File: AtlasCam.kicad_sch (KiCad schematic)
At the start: 36 parts, among them J1 SD_Micro_TFPUSH, J2 USB_C_16Pin_C167321, U1 ESP32-S3-WROOM-1(N8R8), U2 LDO_3V3_2A_AIC1221-33GY3TR, U3 GR6206P282MR-G, U4 GR6206P182MR-G

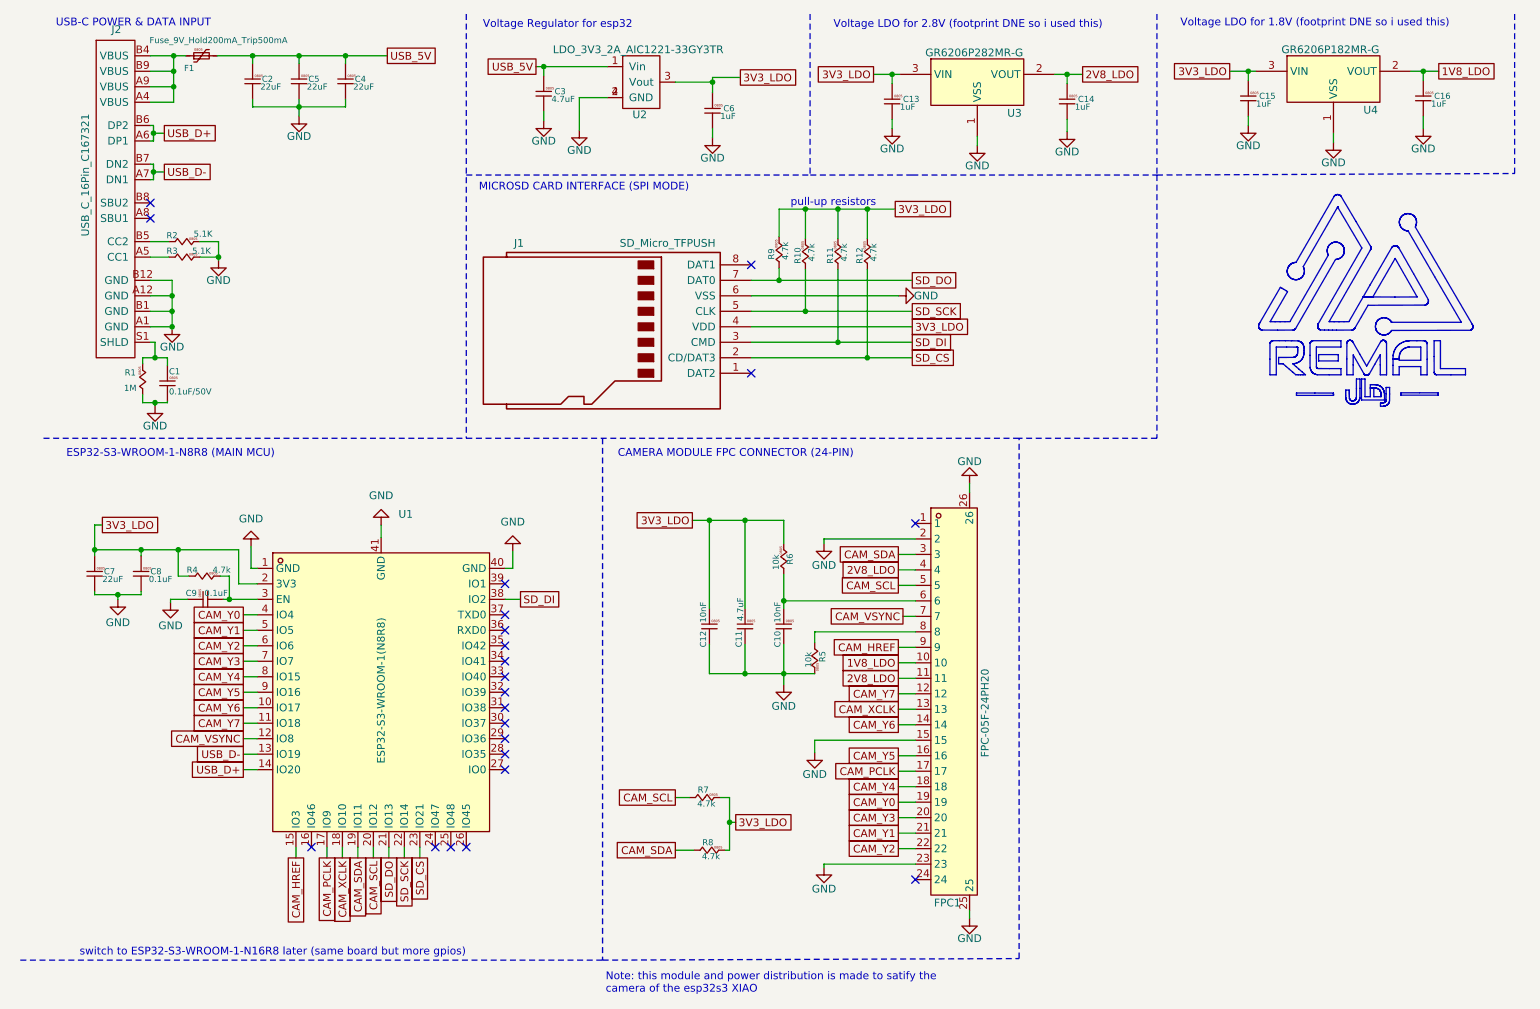
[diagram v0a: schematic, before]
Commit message: First Draft: routiing, pulled D+/D- lines together, SD closer to edge
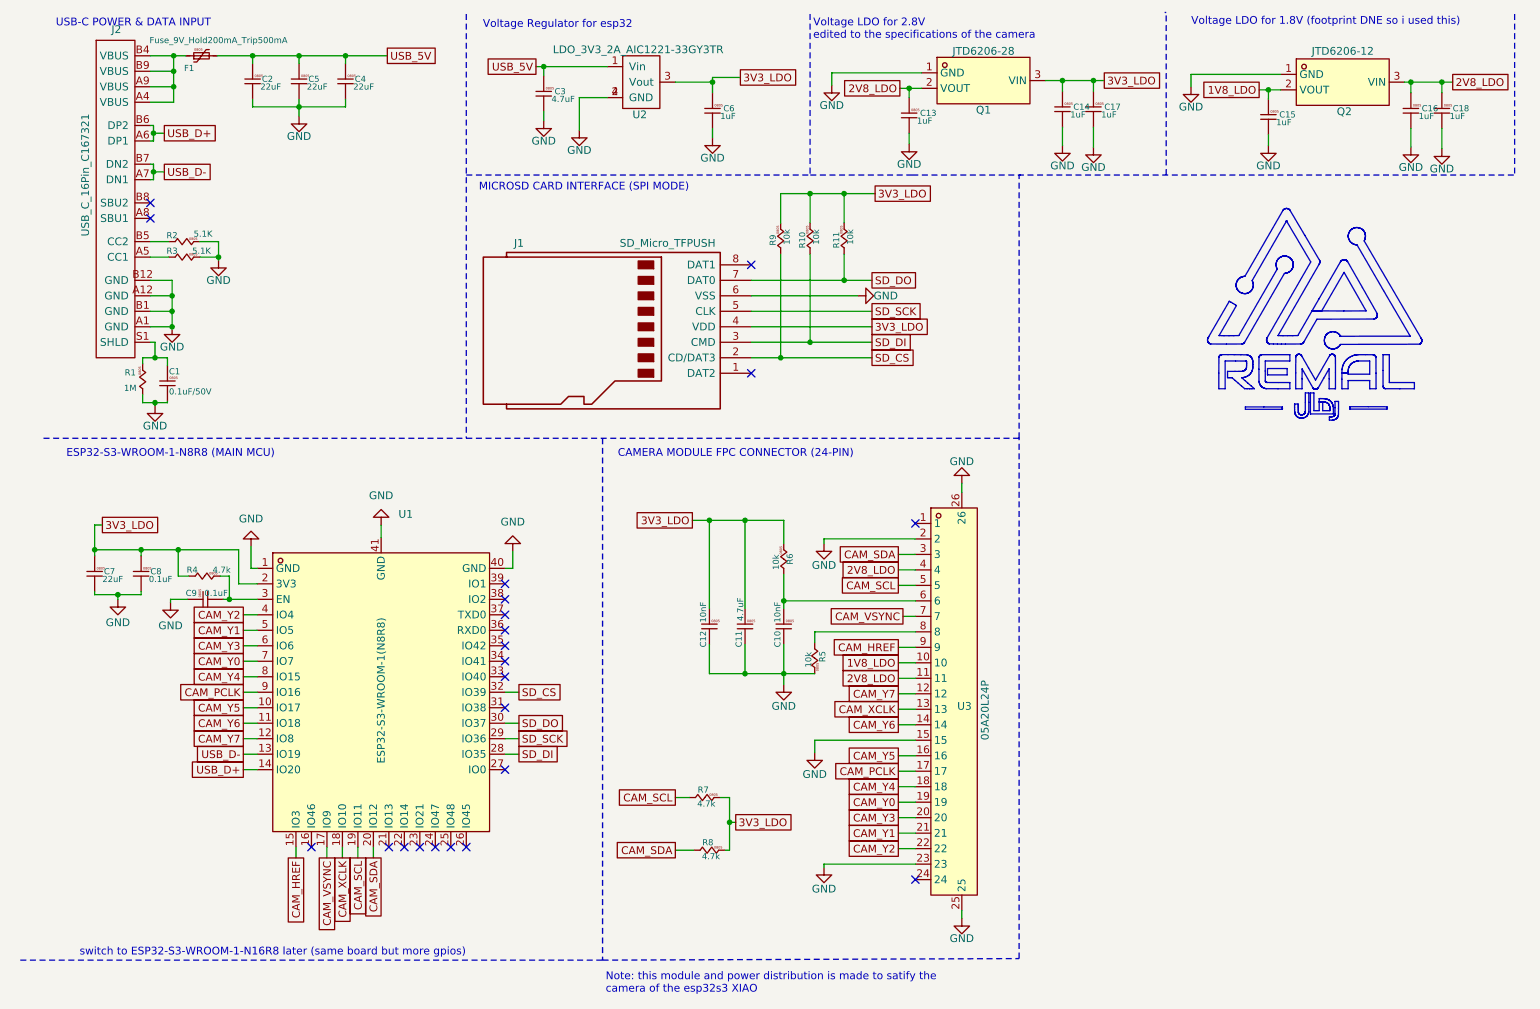
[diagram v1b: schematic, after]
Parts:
- removed FPC1: FPC-05F-24PH20, easyeda2kicad:FPC-SMD_24P-P0.50_FPC-05F-24PH20, symbol easyeda2kicad:FPC-05F-24PH20
- removed R12: 4.7k, Remal_KiCadLib:R_0805_2012m, symbol Remal_KiCadLib:R_0805_2012m
- removed U3: GR6206P282MR-G, easyeda2kicad:SOT-23-3_L2.9-W1.6-P1.90-LS2.8-BR, symbol easyeda2kicad:GR6206P332MR-G
- removed U4: GR6206P182MR-G, easyeda2kicad:SOT-23-3_L2.9-W1.6-P1.90-LS2.8-BR, symbol easyeda2kicad:GR6206P332MR-G
- added C17, C18: 1uF, Remal_KiCadLib:C_0805_2012m, symbol Remal_KiCadLib:C_0805_2012m
- added Q1: JTD6206-28, easyeda2kicad:SOT-23-3_L2.9-W1.3-P1.90-LS2.4-BR, symbol easyeda2kicad:JTD6206-28
- added Q2: JTD6206-12, easyeda2kicad:SOT-23-3_L2.9-W1.3-P1.90-LS2.4-BR, symbol easyeda2kicad:JTD6206-28
- added U3: 05A20L24P, easyeda2kicad:FPC-SMD_24P-P0.50_05A20L24P, symbol easyeda2kicad:05A20L24P
- J2: footprint Remal_KiCadLib:USB_C_16Pin_C167321 -> Remal_KiCadLib:USB_C_16Pin_918-418K2023S40001
- R10, R11, R9: value 4.7k -> 10k
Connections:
- net 1V8_LDO: now also C15.1, Q2.2 (VOUT), U3.10; no longer C16.1
- net 2V8_LDO: now also C13.1, C16.1, C18.1, Q1.2 (VOUT), Q2.3 (VIN), U3.11, U3.4; no longer C14.1
- net 3V3_LDO: now also C14.1, C17.1, Q1.3 (VIN); no longer C13.1, C15.1
- net CAM_HREF: now also U3.9
- net CAM_PCLK: now also U1.9 (IO16), U3.17; no longer U1.17 (IO9)
- net CAM_SCL: now also U1.19 (IO11), U3.5; no longer U1.20 (IO12)
- net CAM_SDA: now also U1.20 (IO12), U3.3; no longer U1.19 (IO11)
- net CAM_VSYNC: now also U1.17 (IO9), U3.7; no longer U1.12 (IO8)
- net CAM_XCLK: now also U3.13
- net CAM_Y0: now also U1.7 (IO7), U3.19; no longer U1.4 (IO4)
- net CAM_Y1: now also U3.21
- net CAM_Y2: now also U1.4 (IO4), U3.22; no longer U1.6 (IO6)
- net CAM_Y3: now also U1.6 (IO6), U3.20; no longer U1.7 (IO7)
- net CAM_Y4: now also U3.18
- net CAM_Y5: now also U1.10 (IO17), U3.16; no longer U1.9 (IO16)
- net CAM_Y6: now also U1.11 (IO18), U3.14; no longer U1.10 (IO17)
- net CAM_Y7: now also U1.12 (IO8), U3.12; no longer U1.11 (IO18)
- net GND: now also C17.2, C18.2, Q1.1 (GND), Q2.1 (GND), U3.15, U3.2, U3.23, U3.25, U3.26
- net SD_CS: now also R9.1, U1.32 (IO39); no longer U1.23 (IO21)
- net SD_DI: now also R10.1, U1.28 (IO35); no longer R11.1, U1.38 (IO2)
- net SD_DO: now also R11.1, U1.30 (IO37); no longer R9.1, U1.21 (IO13)
- net SD_SCK: now also U1.29 (IO36); no longer R10.1, U1.22 (IO14)
- net at R5.1: now also U3.8
- net at C10.1, R6.1: now also U3.6
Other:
- note added: "Voltage LDO for 2.8V edited to the specifications of the camera"
- note removed: "Voltage LDO for 2.8V (footprint DNE so i used this)"
- note removed: "pull-up resistors"
- moved on the sheet: C13, C14

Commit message: Final Updates: pulled D-/D+ closer, moved SD Slot to edge, Verified design
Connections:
- net 1V8_LDO renamed 1V2_LDO
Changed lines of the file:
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@@
 		)
 	)
-	(global_label "1V8_LDO"
+	(global_label "1V2_LDO"
 		(shape passive)
 		(at 211.328 24.638 180)
@@
 		)
 	)
-	(global_label "1V8_LDO"
+	(global_label "1V2_LDO"
 		(shape passive)
 		(at 152.146 118.618 180)
